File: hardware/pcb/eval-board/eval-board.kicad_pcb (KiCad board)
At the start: 2 copper layers, 38 parts, among them J1 Conn_01x02, J2 Conn_01x24, J3 Conn_01x02, J4 Conn_01x02, J5 Conn_01x02, J6 Conn_01x02, J7 Conn_01x02, Q1 Si1308EDL, SW1 SW_SPDT, SW2 SW_SPST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

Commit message: etape intermediaire
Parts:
- moved R4 98.0 mm to (104.1, 110.5), turned to 270 degrees
- moved C2 83.3 mm to (194.3, 113.0), turned to 270 degrees
- moved C1 80.0 mm to (197.5, 113.0), turned to 270 degrees
- moved C3 78.1 mm to (191.1, 113.0), turned to 270 degrees
- moved J2 76.8 mm to (201.3, 94.2), turned to 90 degrees
- moved SW2 76.4 mm to (100.3, 105.4), turned to 270 degrees
- moved C6 74.2 mm to (181.6, 113.0), turned to 270 degrees
- moved C5 74.1 mm to (184.8, 113.0), turned to 270 degrees
- moved J6 71.8 mm to (103.5, 73.7), turned to 90 degrees
- moved C10 69.4 mm to (168.9, 113.0), turned to 270 degrees
- moved J1 69.1 mm to (96.5, 81.3)
- moved C4 68.1 mm to (188.0, 113.0), turned to 270 degrees
- moved C8 67.1 mm to (175.3, 113.0), turned to 270 degrees
- moved C7 65.5 mm to (178.4, 113.0), turned to 270 degrees
- moved C9 65.1 mm to (172.1, 113.0), turned to 270 degrees
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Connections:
- J1 pad 1: GND -> Net-(J1-Pad1)
- J1 pad 2: Net-(J1-Pad2) -> GND
- J3 pad 1: Net-(J1-Pad2) -> Net-(J1-Pad1)
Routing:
- net GND: track 0.00 -> 65.4 mm
- net +BATT: track 0.00 -> 41.7 mm
- net Net-(C15-Pad1): track 0.00 -> 14.8 mm
- net Net-(J1-Pad1): track 0.00 -> 10.9 mm
- net Net-(L2-Pad2): track 0.00 -> 5.27 mm
- net Net-(C14-Pad1): track 0.00 -> 4.24 mm
- net Net-(R3-Pad2): track 0.00 -> 4.20 mm
- net /BUTTON: track 0.00 -> 3.86 mm
- net (no net): vias 0 -> 4
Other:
- board outline added: 117 x 60 mm

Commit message: Carte eval finie
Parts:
- added G***: LOGO, Insa:insa-image, F.Cu at (190.5, 76.2)
- U3: footprint Package_DFN_QFN:DFN-6-1EP_2x2mm_P0.5mm_EP0.61x1.42mm -> Insa:uDFN-6-1EP_2x2mm_P0.65mm_EP1x1.6mm
- moved D3 10.5 mm to (167.6, 91.4)
- moved C11 7.62 mm to (168.9, 87.0)
- moved C12 7.62 mm to (173.4, 81.3)
- moved L1 7.62 mm to (173.4, 87.0)
- moved Q1 7.62 mm to (179.1, 87.0)
- moved R2 7.62 mm to (181.0, 81.3)
- moved D1 7.62 mm to (165.7, 81.3)
- moved D2 7.62 mm to (165.7, 87.0)
- moved R1 7.62 mm to (177.8, 81.3)
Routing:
- net GND: track 65.4 -> 286.7 mm, vias 0 -> 2
- net +2V5: track 0.00 -> 206.1 mm, vias 0 -> 1
- net +BATT: track 41.7 -> 141.9 mm, vias 0 -> 1
- net VD: track 0.00 -> 68.1 mm, vias 0 -> 2
- net /EPD_BUSY: track 0.00 -> 66.5 mm, vias 0 -> 1
- net /EPD_PWRVGL: track 0.00 -> 66.5 mm
- net /BUTTON: track 3.86 -> 65.9 mm, vias 0 -> 1
- net /EPD_VCOM: track 0.00 -> 61.0 mm, vias 0 -> 2
- net /EPD_VSL: track 0.00 -> 60.4 mm, vias 0 -> 2
- net /EPD_RESET: track 0.00 -> 54.9 mm, vias 0 -> 2
- net /~XBEE_SLEEP: track 0.00 -> 52.9 mm
- net /EPD_PWRVGH: track 0.00 -> 51.6 mm
- net /~XBEE_RESET: track 0.00 -> 51.5 mm
- net /USART1_RX: track 0.00 -> 51.1 mm
- net /EPD_CLK: track 0.00 -> 48.2 mm, vias 0 -> 1
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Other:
- board text added: "6/01/2022"
- board text added: "EVAL-E.Ink"
- board text added: "Idd Bat"
- board text added: "Idd Display"
- board text added: "Idd Reg"
- board text added: "Idd STM32"
- board text added: "Idd XBEE"
- board text added: "Ver: 1.0"

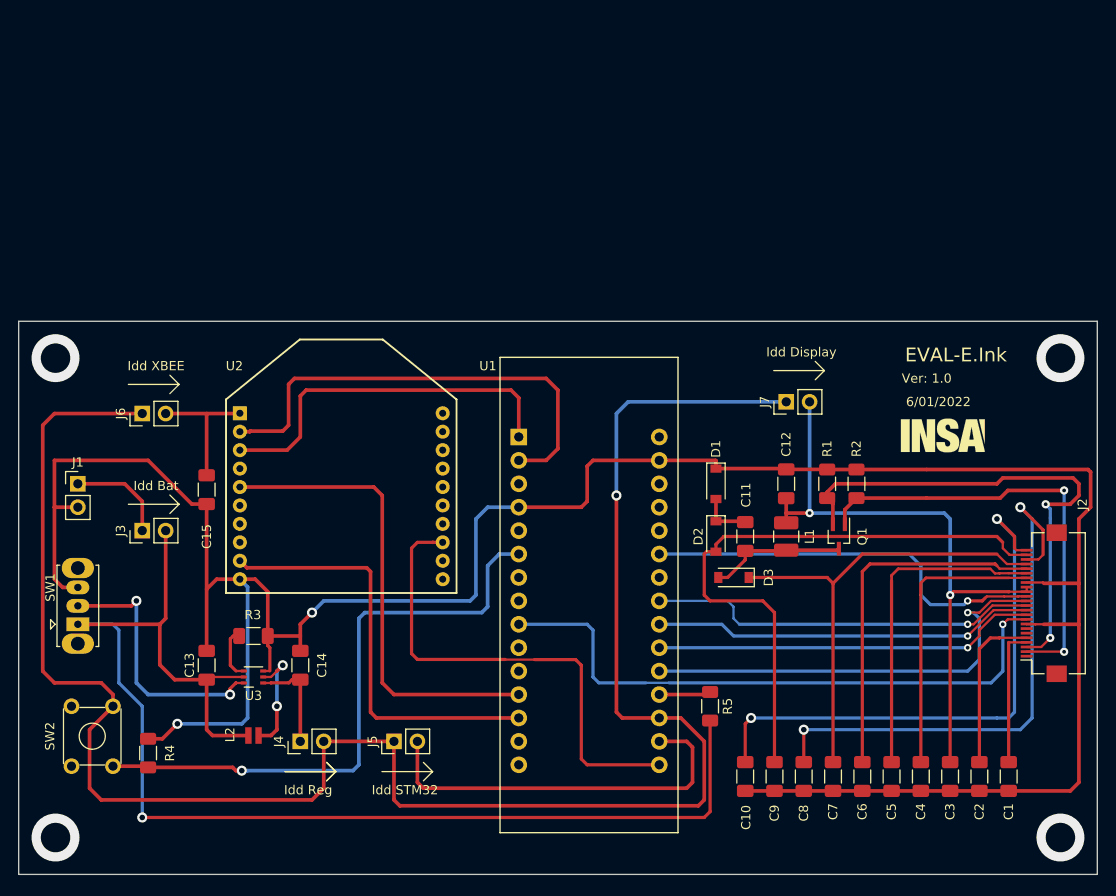
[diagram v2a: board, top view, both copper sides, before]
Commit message: reorganisation de l'arborescence + renommage serveré
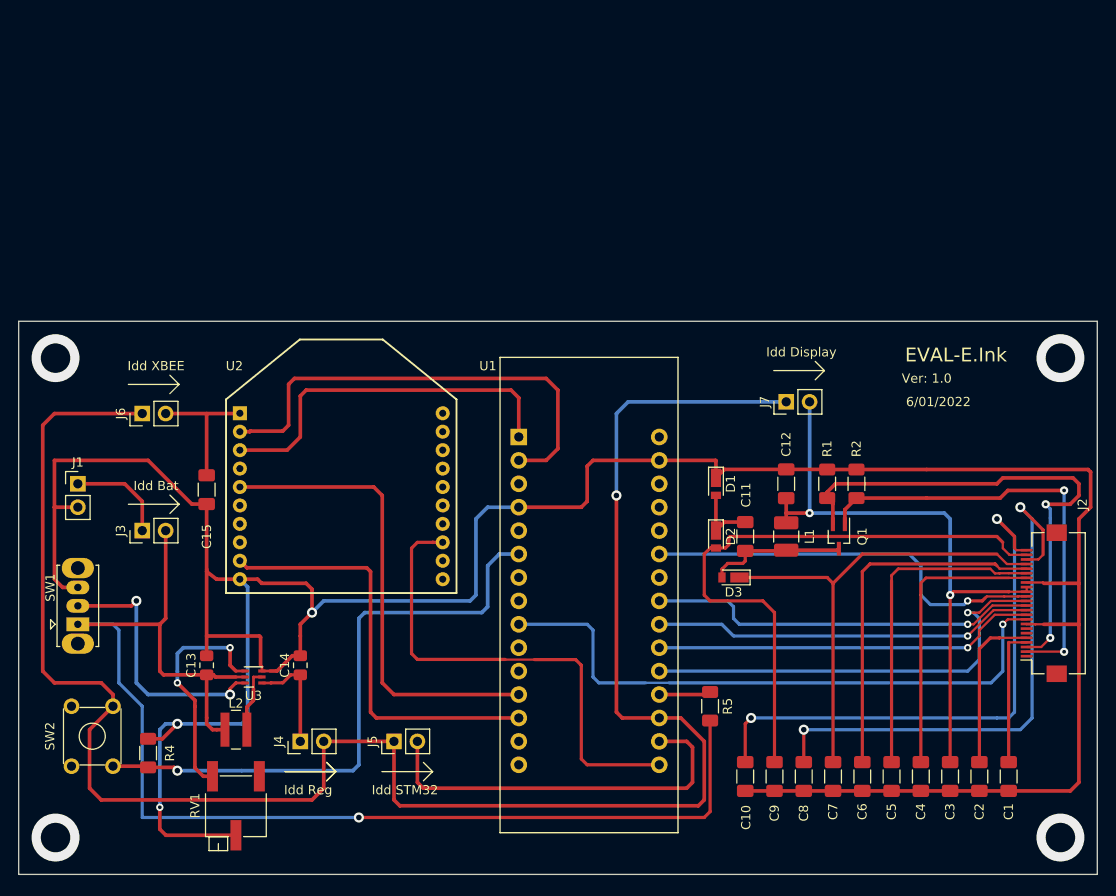
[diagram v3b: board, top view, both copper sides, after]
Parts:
- removed G***: LOGO, Insa:insa-image
- removed R3: R, Resistor_SMD:R_1206_3216Metric_Pad1.30x1.75mm_HandSolder
- added RV1: R_POT_TRIM, Potentiometer_SMD:Potentiometer_Bourns_3269P_Horizontal, F.Cu at (113.7, 116.2)
- C13, C14: footprint Capacitor_SMD:C_1206_3216Metric_Pad1.33x1.80mm_HandSolder -> Capacitor_SMD:C_0805_2012Metric_Pad1.18x1.45mm_HandSolder
- D1, D2, D3: footprint Diode_SMD:D_SOD-123 -> Diode_SMD:D_TUMD2
- L2: footprint Inductor_SMD:L_Wuerth_MAPI-1610 -> Inductor_SMD:L_Wuerth_MAPI-4030
- moved L2 2.01 mm to (113.7, 108.0)
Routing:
- net GND: track 286.7 -> 317.9 mm, vias 2 -> 3
- net Net-(RV1-Pad1): track 5.67 -> 25.1 mm, vias 0 -> 2
- net Net-(L2-Pad2): track 12.4 -> 6.93 mm, vias 2 -> 0
- net +BATT: track 141.9 -> 139.2 mm
